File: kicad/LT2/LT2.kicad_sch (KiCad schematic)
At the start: 29 parts

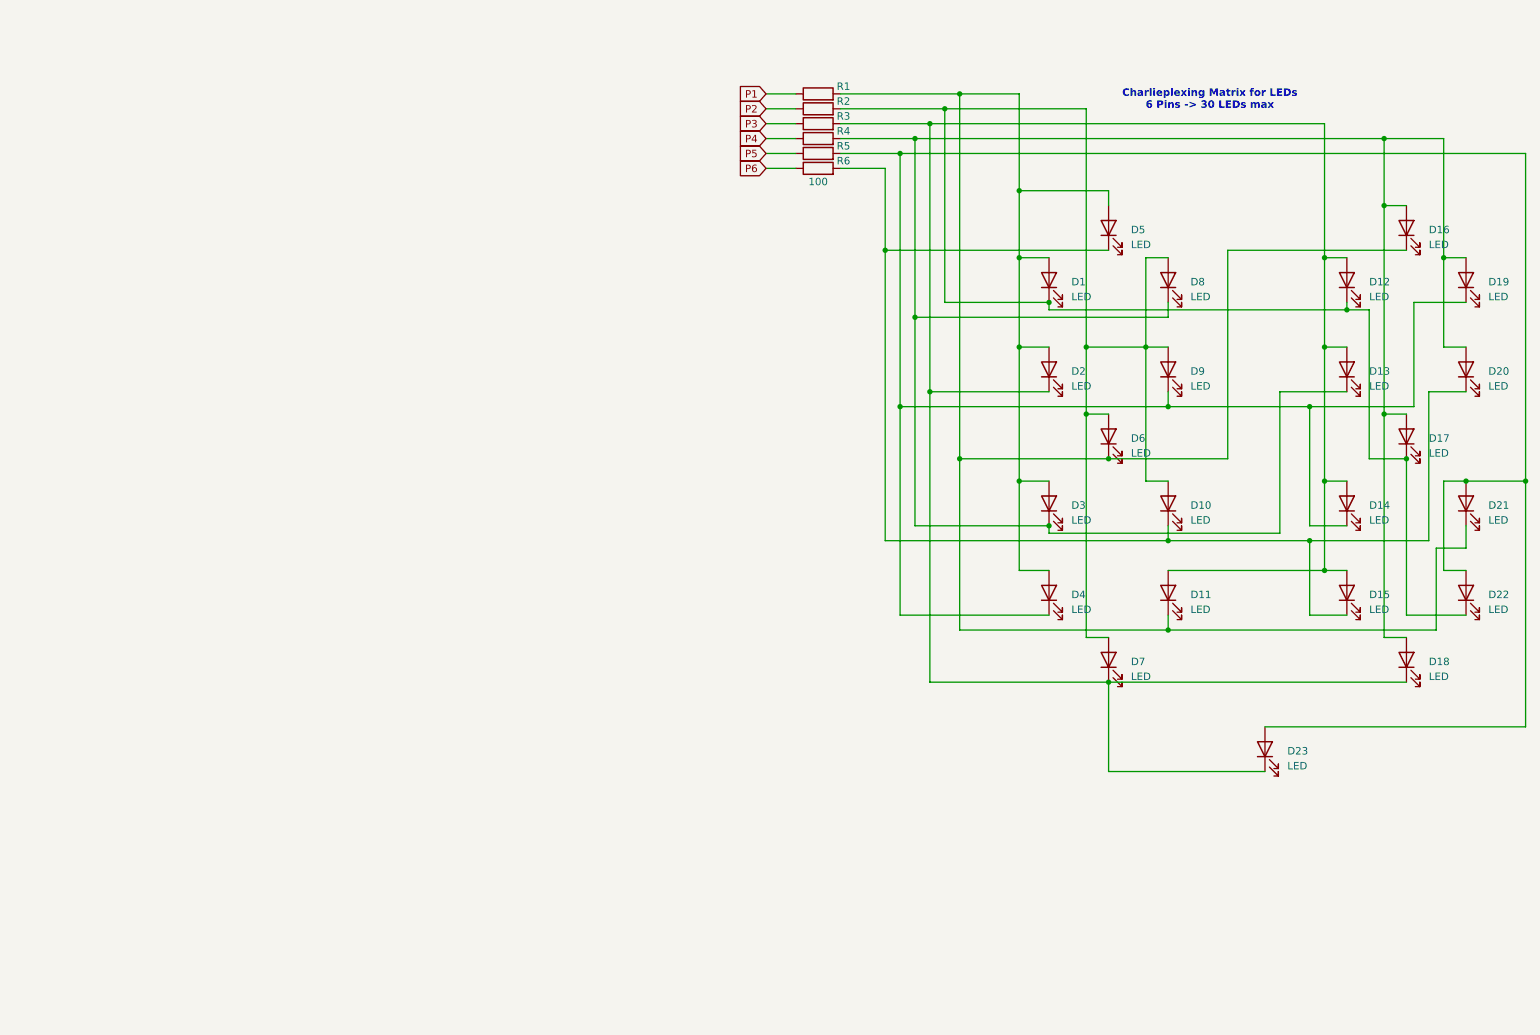
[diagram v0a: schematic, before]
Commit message: placing battey + rot encoder
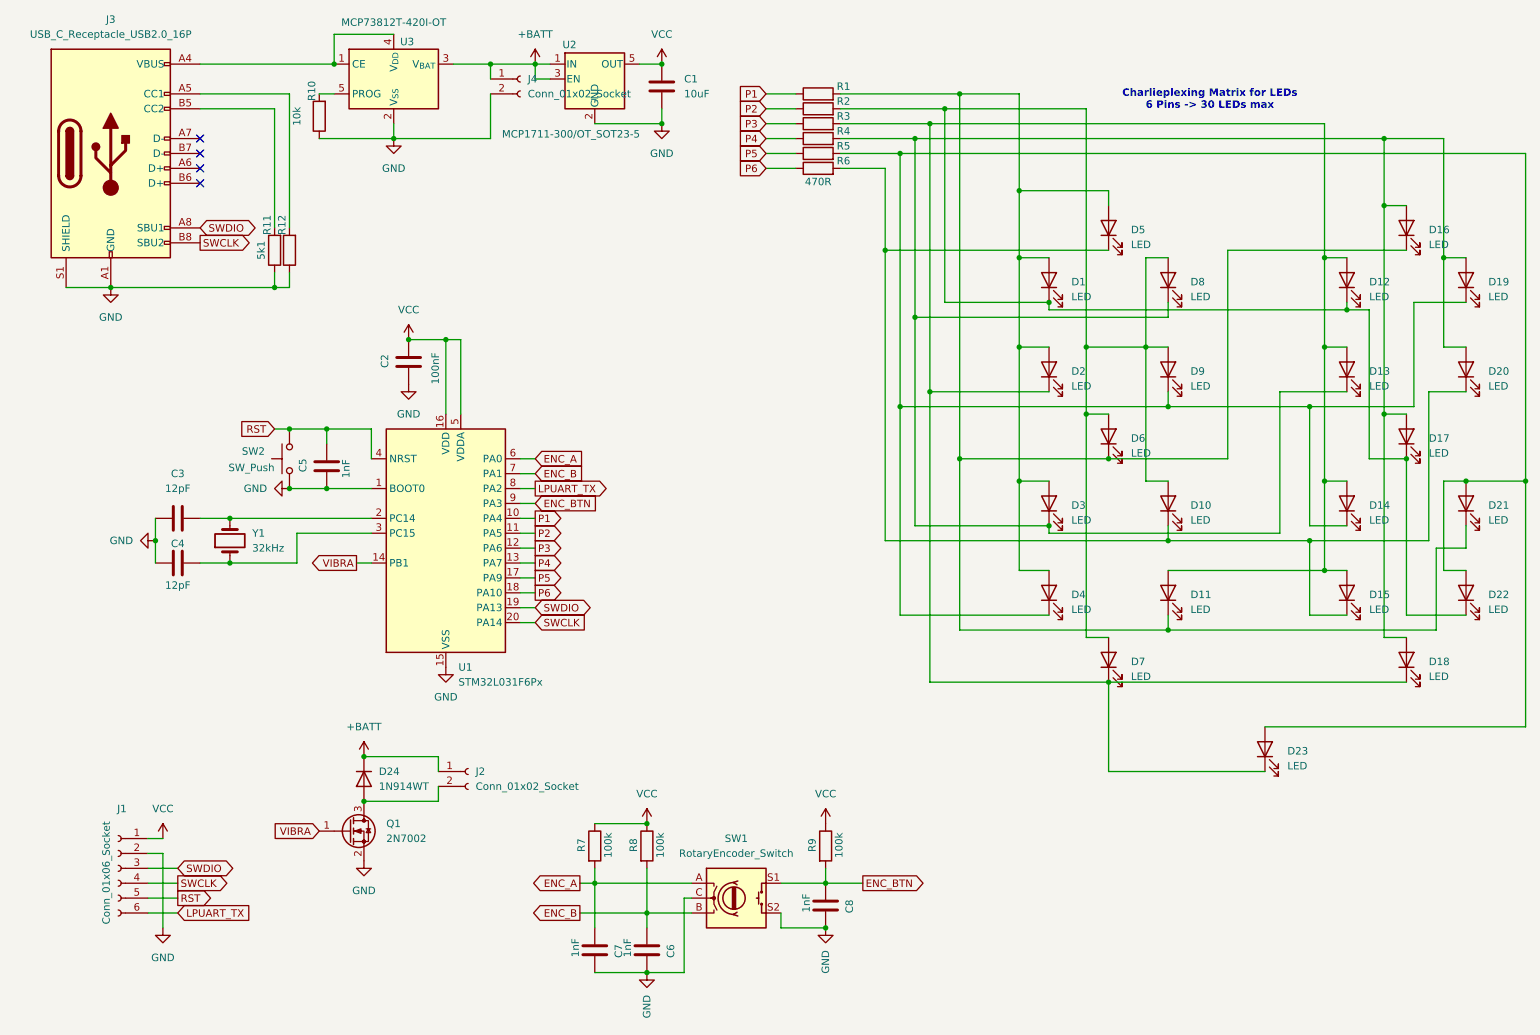
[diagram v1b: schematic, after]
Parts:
- added C1: 10uF, Capacitor_SMD:C_0805_2012Metric, symbol Device:C
- added C2: 100nF, Capacitor_SMD:C_0603_1608Metric, symbol Device:C
- added C3, C4: 12pF, Capacitor_SMD:C_0603_1608Metric, symbol Device:C
- added C5, C6, C7, C8: 1nF, Capacitor_SMD:C_0603_1608Metric, symbol Device:C
- added D24: 1N914WT, Diode_SMD:D_SOD-523, symbol Diode:1N914WT
- added J1: Conn_01x06_Socket, Connector_PinHeader_1.27mm:PinHeader_1x06_P1.27mm_Vertical, symbol Connector:Conn_01x06_Socket
- added J2, J4: Conn_01x02_Socket, Connector_PinHeader_1.27mm:PinHeader_1x02_P1.27mm_Vertical, symbol Connector:Conn_01x02_Socket
- added J3: USB_C_Receptacle_USB2.0_16P, Connector_USB:USB_C_Receptacle_G-Switch_GT-USB-7010ASV, symbol Connector:USB_C_Receptacle_USB2.0_16P
- added Q1: 2N7002, Package_TO_SOT_SMD:SOT-23, symbol Transistor_FET:2N7002
- added R10: 10k, Resistor_SMD:R_0603_1608Metric, symbol Device:R
- added R11, R12: 5k1, Resistor_SMD:R_0603_1608Metric, symbol Device:R
- added R7, R8, R9: 100k, Resistor_SMD:R_0603_1608Metric, symbol Device:R
- added SW1: RotaryEncoder_Switch, LT2:rotary_encoder_PEC11S-929K, symbol Device:RotaryEncoder_Switch
- added SW2: SW_Push, Button_Switch_THT:SW_TH_Tactile_Omron_B3F-100x, symbol Switch:SW_Push
- added U1: STM32L031F6Px, Package_SO:TSSOP-20_4.4x6.5mm_P0.65mm, symbol MCU_ST_STM32L0:STM32L031F6Px
- added U2: MCP1711-300/OT_SOT23-5, Package_TO_SOT_SMD:SOT-23-5, symbol Regulator_Linear:TLV71209_SOT23-5
- added U3: MCP73812T-420I-OT, Package_TO_SOT_SMD:SOT-23-5, symbol Battery_Management:MCP73812T-420I-OT
- added Y1: 32kHz, Crystal:Crystal_SMD_3215-2Pin_3.2x1.5mm, symbol Device:Crystal
- R1, R2, R3, R4, R5, R6: value 100 -> 470R; footprint (none) -> Resistor_SMD:R_0603_1608Metric
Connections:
- net P1: now also U1.10 (PA4)
- net P2: now also U1.11 (PA5)
- net P3: now also U1.12 (PA6)
- net P4: now also U1.13 (PA7)
- net P5: now also U1.17 (PA9)
- net P6: now also U1.18 (PA10)
- new net: J3.A5 (CC1), R12.2
- new net: D24.2 (A), J2.2 (Pin_2), Q1.3 (D)
- new net: C3.2, U1.2 (PC14), Y1.2
- new net: C4.2, U1.3 (PC15), Y1.1
- new net: J3.A4 (VBUS), J3.A9 (VBUS), J3.B4 (VBUS), J3.B9 (VBUS), U3.1 (CE), U3.4 (V_{DD})
- new net: R10.2, U3.5 (PROG)
- new net: J3.B5 (CC2), R11.2
- new net +BATT: D24.1 (K), J2.1 (Pin_1), J4.1 (Pin_1), U2.1 (IN), U2.3 (EN), U3.3 (V_{BAT})
- new net ENC_A: C7.2, R7.2, SW1.A, U1.6 (PA0)
- new net ENC_B: C6.2, R8.2, SW1.B, U1.7 (PA1)
- new net ENC_BTN: C8.2, R9.2, SW1.S1, U1.9 (PA3)
- new net GND: C1.2, C2.2, C3.1, C4.1, C5.2, C6.1, C7.1, C8.1, J1.2 (Pin_2), J3.A1 (GND), J3.A12 (GND), J3.B1 (GND), J3.B12 (GND), J3.S1 (SHIELD), J4.2 (Pin_2), Q1.2 (S), R10.1, R11.1, R12.1, SW1.C, SW1.S2, SW2.1, U1.1 (BOOT0), U1.15 (VSS), U2.2 (GND), U3.2 (V_{SS})
- new net LPUART_TX: J1.6 (Pin_6), U1.8 (PA2)
- new net RST: C5.1, J1.5 (Pin_5), SW2.2, U1.4 (NRST)
- new net SWCLK: J1.4 (Pin_4), J3.B8 (SBU2), U1.20 (PA14)
- new net SWDIO: J1.3 (Pin_3), J3.A8 (SBU1), U1.19 (PA13)
- new net VCC: C1.1, C2.1, J1.1 (Pin_1), R7.1, R8.1, R9.1, U1.16 (VDD), U1.5 (VDDA), U2.5 (OUT)
- new net VIBRA: Q1.1 (G), U1.14 (PB1)
- no-connect marks 0 -> 4
